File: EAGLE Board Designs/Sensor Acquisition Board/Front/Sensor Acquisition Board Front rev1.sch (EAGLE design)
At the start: 36 parts, among them J1 CONNECTOR-SENSOR_NF_S_RA_BLACK, J10 JUMPER_0603_, J2 CONNECTOR-SENSOR_NF_S_RA_BLACK, J3 CONNECTOR-CAN_NF_S_RA_BLACK, J4 CONNECTOR-CAN_NF_S_RA_BLACK, J6 JUMPER_0603_, U1 VOLTAGE_REGULATOR_SOT-223_5V, U2 MCP2562FD, U3 MCP2562FD

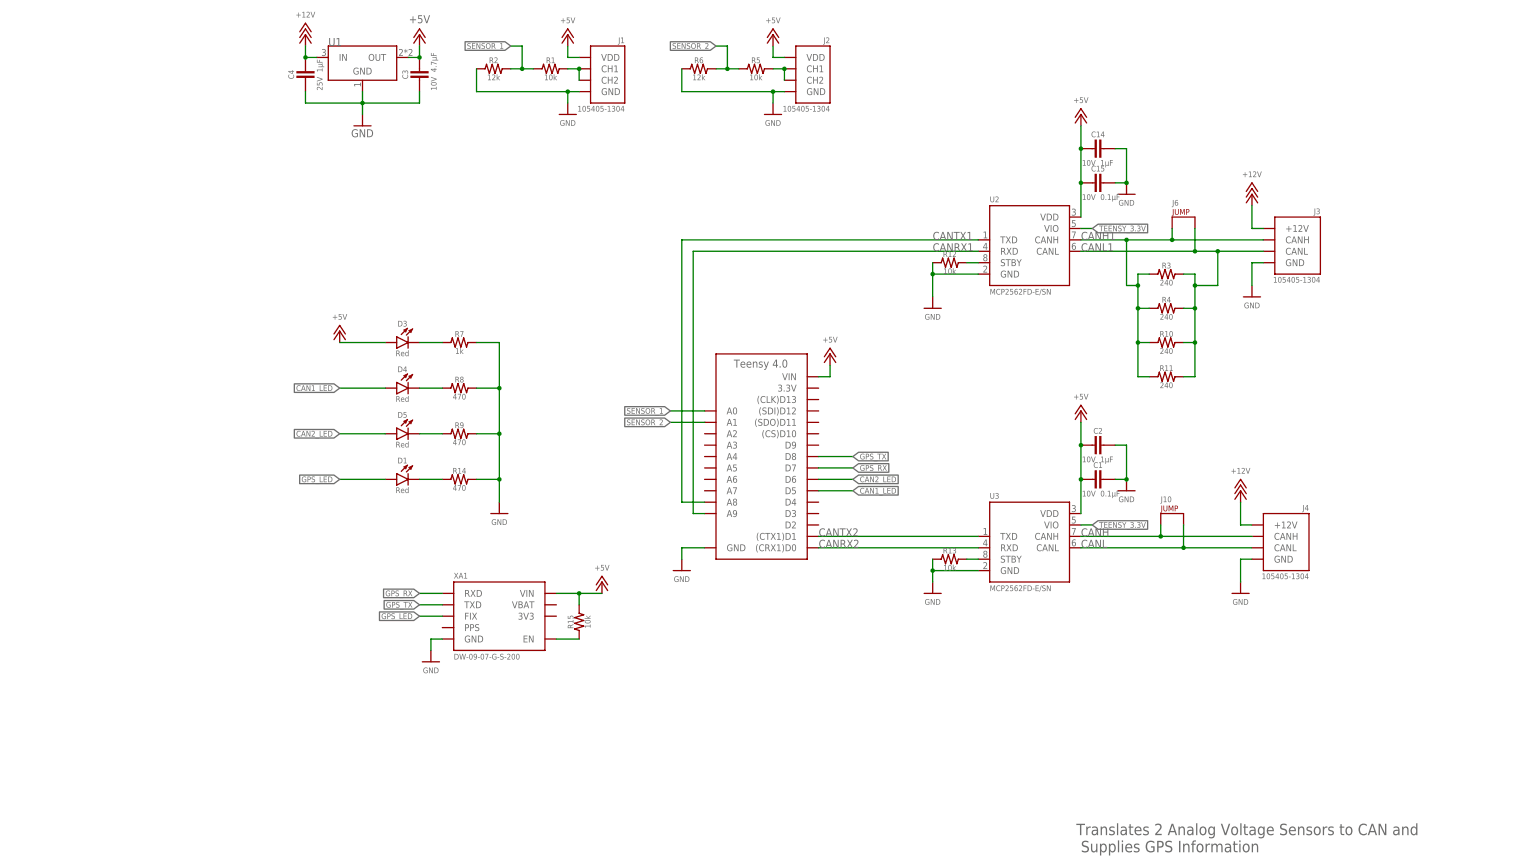
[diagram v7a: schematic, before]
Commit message: corrected Nanofits to Microfits and order files
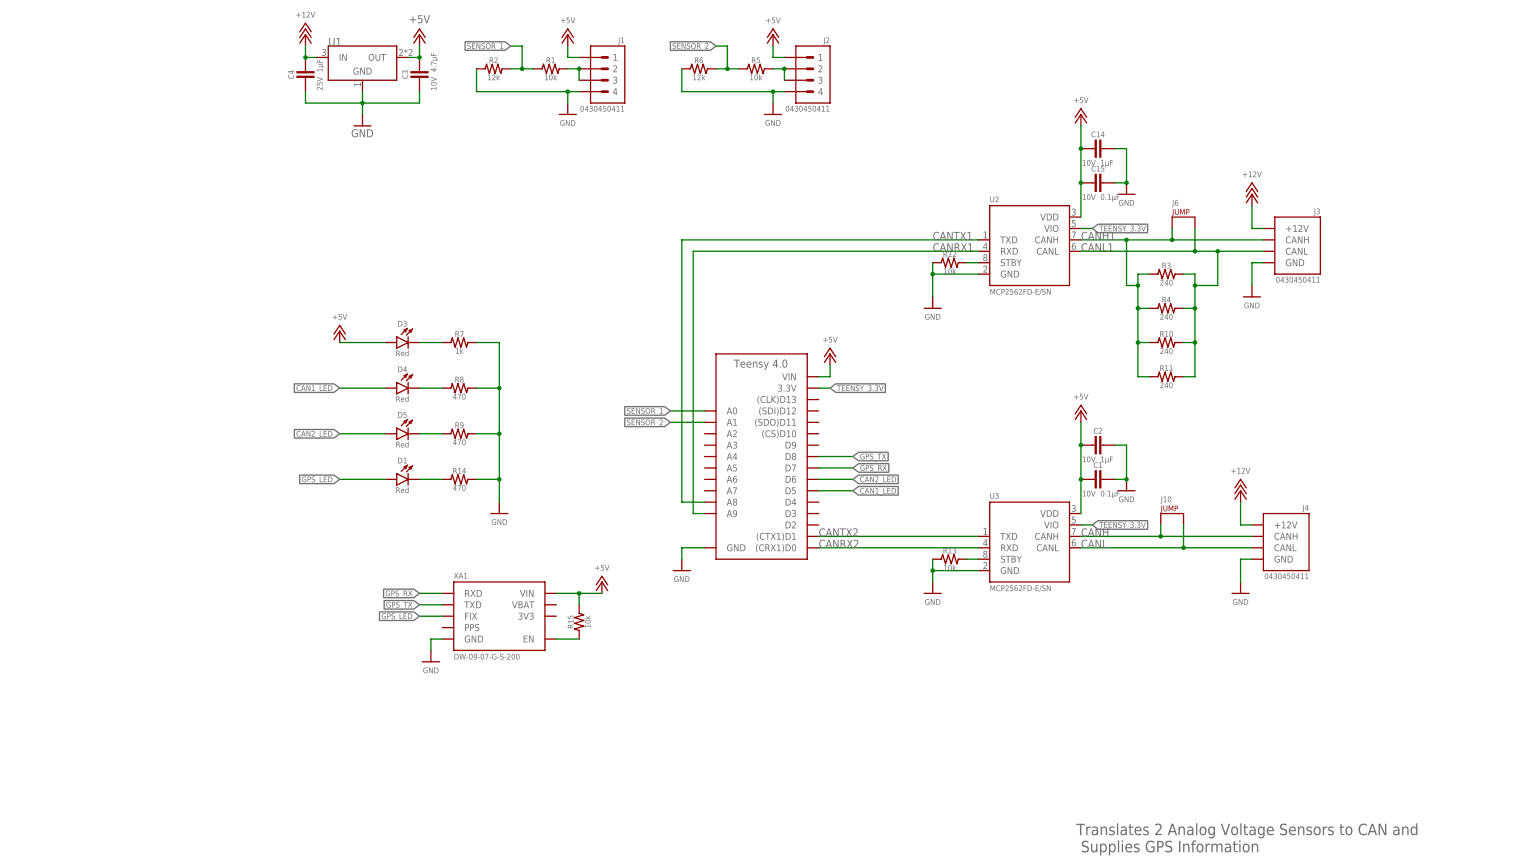
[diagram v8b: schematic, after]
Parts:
- J1, J2: value CONNECTOR-SENSOR_NF_S_RA_BLACK -> CONNECTOR-4_μF_S_RA_; device HyTechDevices:CONNECTOR-SENSOR_NF_S_RA_BLACK -> HyTechDevices:CONNECTOR-4_μF_S_RA_
- J3, J4: value CONNECTOR-CAN_NF_S_RA_BLACK -> CONNECTOR-CAN_μF_S_RA_; device HyTechDevices:CONNECTOR-CAN_NF_S_RA_BLACK -> HyTechDevices:CONNECTOR-CAN_μF_S_RA_
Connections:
- net +5V: now also J1.1, J2.1; no longer J1.VDD, J2.VDD
- net GND: now also J1.4, J2.4; no longer J1.GND, J2.GND
- net N$11: now also J2.2, J2.3; no longer J2.CH1, J2.CH2
- net N$8: now also J1.2, J1.3; no longer J1.CH1, J1.CH2
- net TEENSY_3.3V: now also A2.3.3V
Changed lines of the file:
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@@
 <part name="P8" library="HyTechSupplies" deviceset="+12V" device=""/>
 <part name="J10" library="HyTechDevices" deviceset="JUMPER_?_*" device="0603"/>
-<part name="J1" library="HyTechDevices" deviceset="CONNECTOR-SENSOR_?_*" device="NF_S_RA" technology="BLACK"/>
-<part name="J2" library="HyTechDevices" deviceset="CONNECTOR-SENSOR_?_*" device="NF_S_RA" technology="BLACK"/>
+<part name="J1" library="HyTechDevices" deviceset="CONNECTOR-4_?_*" device="μF_S_RA"/>
+<part name="J2" library="HyTechDevices" deviceset="CONNECTOR-4_?_*" device="μF_S_RA"/>
 <part name="P4" library="HyTechSupplies" deviceset="+5V" device=""/>
 <part name="P5" library="HyTechSupplies" deviceset="+5V" device=""/>
@@
 <part name="C14" library="HyTechDevices" deviceset="CAPACITOR_?_*" device="0603" technology="10V_1UF"/>
 <part name="P13" library="HyTechSupplies" deviceset="GND" device=""/>
-<part name="J3" library="HyTechDevices" deviceset="CONNECTOR-CAN_?_*" device="NF_S_RA" technology="BLACK"/>
+<part name="J3" library="HyTechDevices" deviceset="CONNECTOR-CAN_?_*" device="μF_S_RA" value="CONNECTOR-CAN_μF_S_RA_"/>
 <part name="P14" library="HyTechSupplies" deviceset="GND" device=""/>
 <part name="P18" library="HyTechSupplies" deviceset="+12V" device=""/>
@@
 <part name="R10" library="HyTechDevices" deviceset="RESISTOR_?_*" device="0603" technology="240"/>
 <part name="R11" library="HyTechDevices" deviceset="RESISTOR_?_*" device="0603" technology="240"/>
-<part name="J4" library="HyTechDevices" deviceset="CONNECTOR-CAN_?_*" device="NF_S_RA" technology="BLACK"/>
+<part name="J4" library="HyTechDevices" deviceset="CONNECTOR-CAN_?_*" device="μF_S_RA" value="CONNECTOR-CAN_μF_S_RA_"/>
 <part name="U2" library="HyTechDevices" deviceset="MCP2562FD" device=""/>
 <part name="U3" library="HyTechDevices" deviceset="MCP2562FD" device=""/>
@@
 </segment>
 <segment>
-<pinref part="J2" gate="G$1" pin="GND"/>
+<pinref part="J2" gate="G$1" pin="4"/>
 <wire x1="132.08" y1="180.34" x2="129.54" y2="180.34" width="0.1524" layer="91"/>
 <wire x1="129.54" y1="180.34" x2="129.54" y2="177.8" width="0.1524" layer="91"/>
@@
 </segment>
 <segment>
-<pinref part="J1" gate="G$1" pin="GND"/>
+<pinref part="J1" gate="G$1" pin="4"/>
 <pinref part="R2" gate="G$1" pin="1"/>
 <wire x1="63.5" y1="185.42" x2="63.5" y2="180.34" width="0.1524" layer="91"/>
@@
 </segment>
 <segment>
-<pinref part="J1" gate="G$1" pin="VDD"/>
+<pinref part="J1" gate="G$1" pin="1"/>
 <wire x1="86.36" y1="187.96" x2="83.82" y2="187.96" width="0.1524" layer="91"/>
 <wire x1="83.82" y1="187.96" x2="83.82" y2="190.5" width="0.1524" layer="91"/>
@@
 </segment>
 <segment>
-<pinref part="J2" gate="G$1" pin="VDD"/>
+<pinref part="J2" gate="G$1" pin="1"/>
 <wire x1="132.08" y1="187.96" x2="129.54" y2="187.96" width="0.1524" layer="91"/>
 <wire x1="129.54" y1="187.96" x2="129.54" y2="190.5" width="0.1524" layer="91"/>
@@
 <wire x1="198.12" y1="149.86" x2="200.66" y2="149.86" width="0.1524" layer="91"/>
 </segment>
+<segment>
+<pinref part="A2" gate="G$1" pin="3.3V"/>
+<wire x1="139.7" y1="114.3" x2="142.24" y2="114.3" width="0.1524" layer="91"/>
+<label x="142.24" y="114.3" size="1.27" layer="95" xref="yes"/>
+</segment>
 </net>
 <net name="SENSOR_1" class="0">
@@
 <segment>
 <pinref part="R1" gate="G$1" pin="2"/>
-<pinref part="J1" gate="G$1" pin="CH1"/>
+<pinref part="J1" gate="G$1" pin="2"/>
 <wire x1="83.82" y1="185.42" x2="86.36" y2="185.42" width="0.1524" layer="91"/>
-<pinref part="J1" gate="G$1" pin="CH2"/>
+<pinref part="J1" gate="G$1" pin="3"/>
 <wire x1="86.36" y1="185.42" x2="86.36" y2="182.88" width="0.1524" layer="91"/>
 <junction x="86.36" y="185.42"/>
@@
 <segment>
 <pinref part="R5" gate="G$1" pin="2"/>
-<pinref part="J2" gate="G$1" pin="CH1"/>
+<pinref part="J2" gate="G$1" pin="2"/>
 <wire x1="129.54" y1="185.42" x2="132.08" y2="185.42" width="0.1524" layer="91"/>
-<pinref part="J2" gate="G$1" pin="CH2"/>
+<pinref part="J2" gate="G$1" pin="3"/>
 <wire x1="132.08" y1="185.42" x2="132.08" y2="182.88" width="0.1524" layer="91"/>
 <junction x="132.08" y="185.42"/>
